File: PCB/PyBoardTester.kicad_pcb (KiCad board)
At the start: 4 copper layers, 113.5 x 114.7 mm, 113 parts, among them J1 6pin_hd, J2 Conn_01x08, J3 Conn_01x08, J4 3pin_hd, J5 USB4105-GF-A, SW1 SW_SPST, U1 THS4281, U3 THS4281, U4 ATXMEGA32A4U-MH, U5 THS4281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

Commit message: modificado power-jumper
- passou a ser solder-jumper
- default: ligado a USB-Power
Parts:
- J4: footprint Connector_PinHeader_2.54mm:PinHeader_1x03_P2.54mm_Vertical -> Jumper:SolderJumper-3_P1.3mm_Bridged12_RoundedPad1.0x1.5mm
- moved J4 2.60 mm to (175.7, 118.5), turned to 180 degrees
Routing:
- net USB+5V: track 15.7 -> 17.1 mm
- net V+#2: track 97.7 -> 98.9 mm, vias 2 -> 3

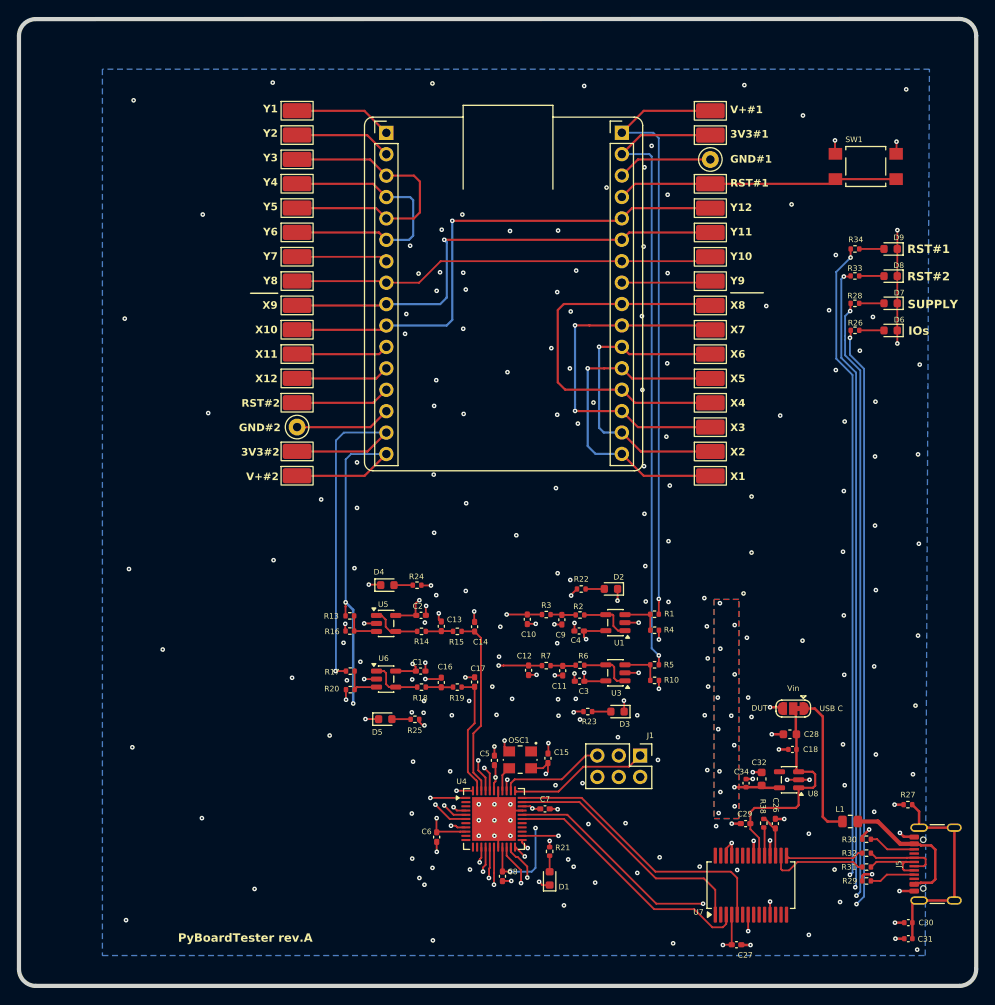
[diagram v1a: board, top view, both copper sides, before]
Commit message: após revisão do Filipe
- adicionados LEDs PASS & FAIL para sinalizar fim teste
- modificadasa Designators de LEDs para estar coerente na BOM
- unidos pares de IOs do pyBoard q faltavam
- reimensionado divisor resistivo para ADC-In
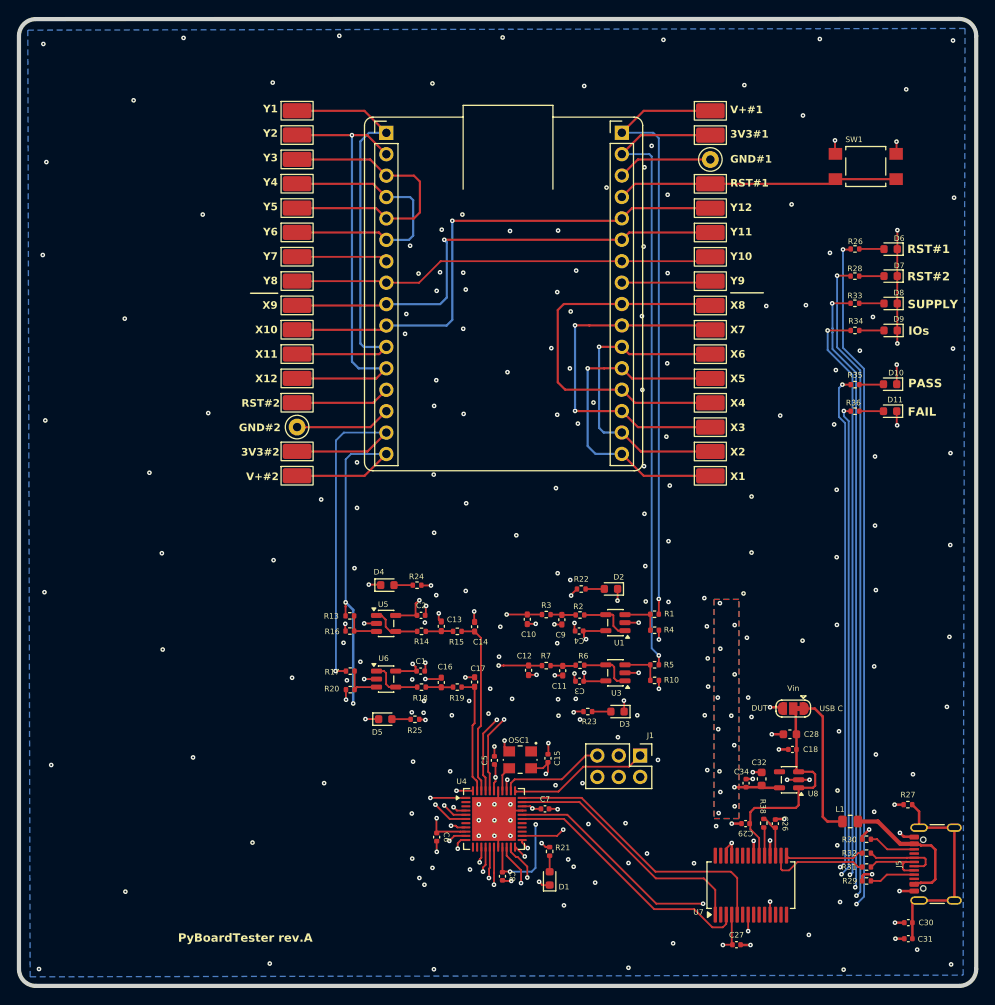
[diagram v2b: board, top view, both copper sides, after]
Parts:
- added D10: Green LED, LED_SMD:LED_0603_1608Metric, F.Cu at (187.1, 80.0)
- added D11: Red LED, LED_SMD:LED_0603_1608Metric, F.Cu at (187.1, 83.2)
- added R35: 330R, Resistor_SMD:R_0402_1005Metric, F.Cu at (183.0, 80.1)
- added R36: 560, Resistor_SMD:R_0402_1005Metric, F.Cu at (183.0, 83.2)
- C1, C15, C2, C26, C27, C29, C3, C4, C5, C6, C7, C8: footprint Capacitor_SMD:C_0402_1005Metric_Pad0.74x0.62mm_HandSolder -> Capacitor_SMD:C_0402_1005Metric
- D1: value STATE-LED -> Green LED
- D2: value A-PWR -> Green LED
- D3: value B-PWR -> Green LED
- D4: value C-PWR -> Green LED
- D5, D6, D7, D8, D9: value D-PWR -> Green LED
- R10, R16, R20, R4: value 10k -> 5k1
- R21, R22, R23, R24, R25, R26, R28, R33, R34: value 560R -> 330R
- R29, R30: value 5.1k -> 5k1
- moved D9 9.67 mm to (187.2, 73.7)
- moved R34 9.67 mm to (183.0, 73.7)
- moved D6 9.65 mm to (187.2, 64.0)
- moved R26 9.65 mm to (183.0, 64.0)
- moved D8 3.24 mm to (187.2, 70.5)
- moved R33 3.24 mm to (183.0, 70.4)
- moved D7 3.23 mm to (187.2, 67.2)
- moved R28 3.23 mm to (183.0, 67.2)
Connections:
- J2 pad 1: /module on test/PC6-Y1 -> /module on test/PC4-X11
- J2 pad 2: /module on test/PC7-Y2 -> /module on test/PC5-X12
- TP1 pad 1: /module on test/PC6-Y1 -> /module on test/PC4-X11
- TP3 pad 1: /module on test/PC7-Y2 -> /module on test/PC5-X12
- U4 pad 10: unconnected-(U4-PC0/OC0A/SDA-Pad10) -> /OK_LED
- U4 pad 11: unconnected-(U4-PC1/OC0B/XCK0/SCL-Pad11) -> /NOK_LED
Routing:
- net /OK_LED: track 0.00 -> 109.8 mm, vias 0 -> 3
- net /NOK_LED: track 0.00 -> 106.0 mm, vias 0 -> 3
- net /module on test/PC5-X12: track 11.1 -> 53.9 mm, vias 0 -> 1
- net /module on test/PC4-X11: track 10.9 -> 53.3 mm
- net /module on test/PC6-Y1: track 11.7 -> 0.00 mm
- net /module on test/PC7-Y2: track 11.5 -> 0.00 mm
- net /RST#1_LED: track 115.0 -> 125.8 mm
- net /IOs_LED: track 117.1 -> 109.9 mm
- net /RST#2_LED: track 116.0 -> 121.0 mm
- net GND: track 107.4 -> 111.5 mm, vias 228 -> 244
- net Net-(D10-A): track 0.00 -> 2.89 mm
- net Net-(D11-A): track 0.00 -> 2.86 mm
- net /SUPPLY_LED: track 116.8 -> 115.3 mm
- net /STATE_LED: track 13.5 -> 14.8 mm
- net /V+#1_chck: track 26.6 -> 26.0 mm
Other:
- board text added: "FAIL"
- board text added: "PASS"
